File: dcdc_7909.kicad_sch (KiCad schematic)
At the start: 48 parts, among them J1 V_IN, J2 G_IN, J3 Conn_01x01, J4 Conn_01x01, J5 Conn_01x01, J6 Conn_01x01, J7 +10V, J8 G_OUT, J9 -10V, U1 LM2940-SOT223-15, U2 MAX764, U3 LT3045xMSE, U4 LT3094xMSE

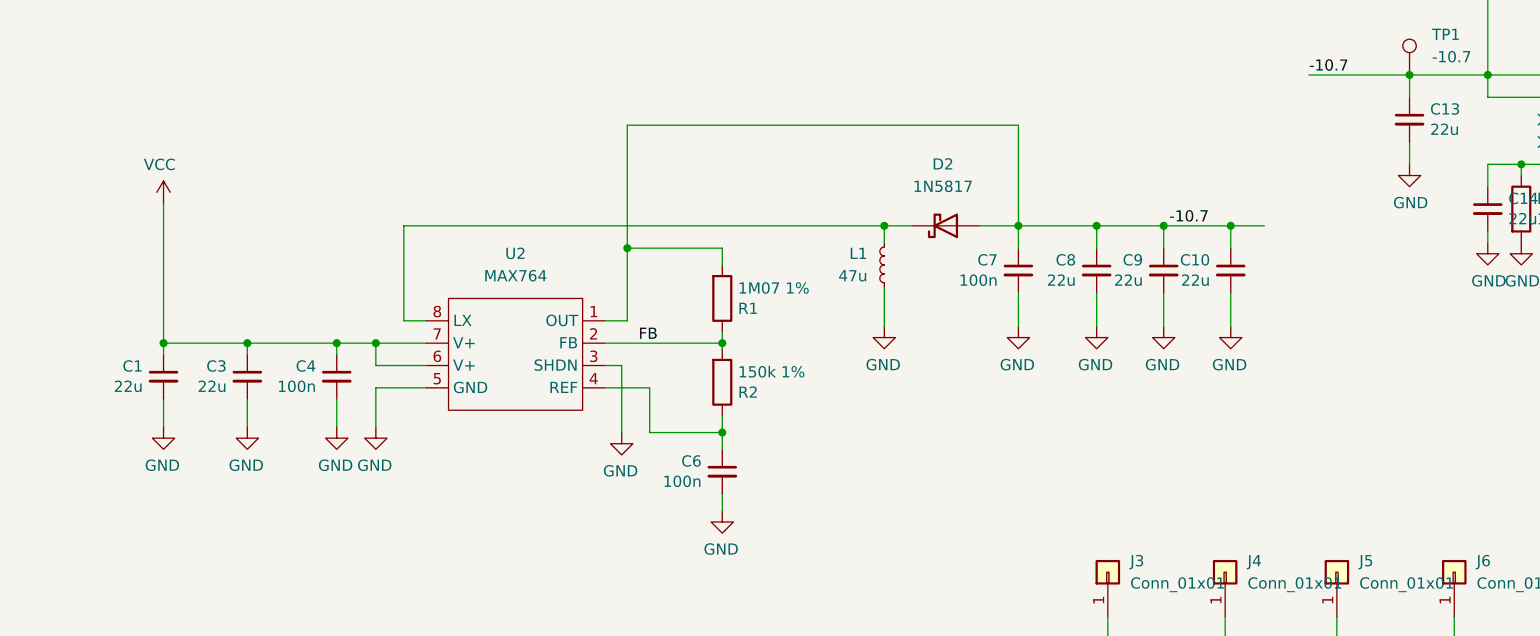
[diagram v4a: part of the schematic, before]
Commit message: Ready design, but MAX764 cannot be used because of the Vin-Vout differential.
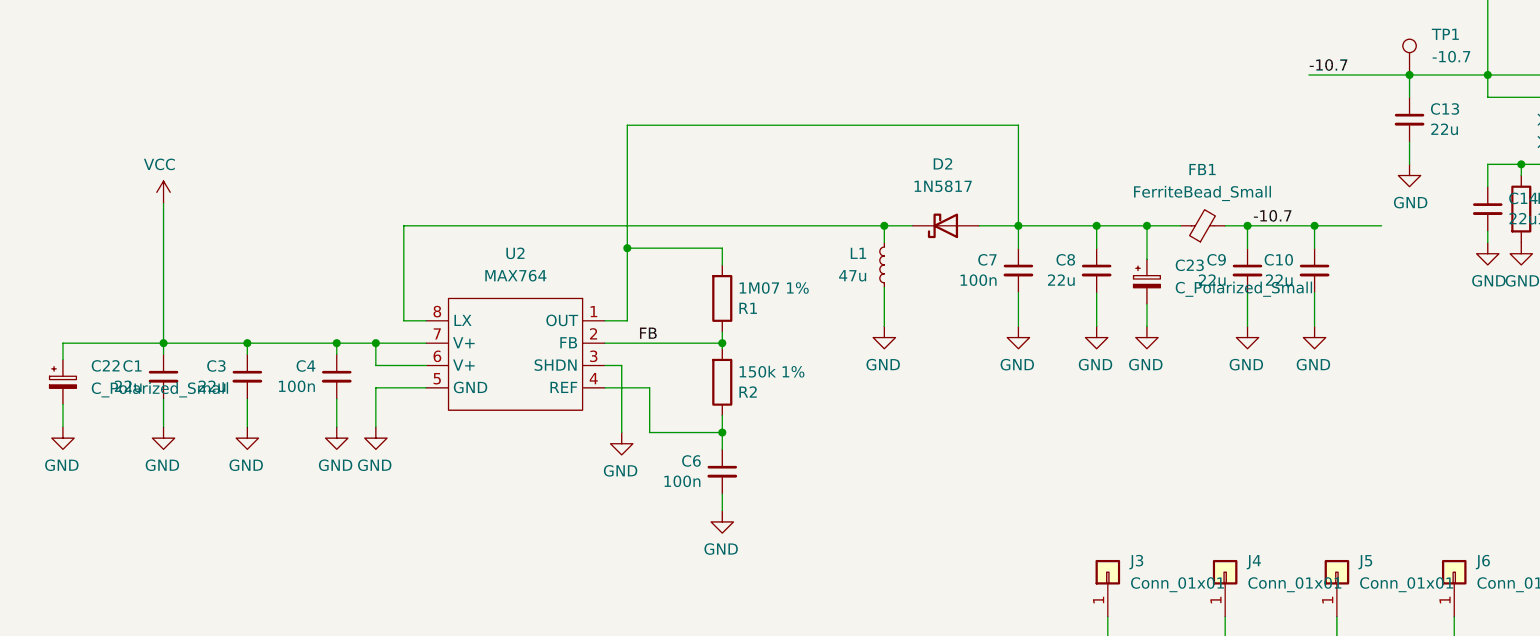
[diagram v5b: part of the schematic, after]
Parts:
- added C22, C23: C_Polarized_Small, Capacitor_Tantalum_SMD:CP_EIA-7343-31_Kemet-D_Pad2.25x2.55mm_HandSolder, symbol Device:C_Polarized_Small
- added FB1: FerriteBead_Small, Resistor_SMD:R_0805_2012Metric, symbol Device:FerriteBead_Small
- D2: LCSC (none) -> C155287
- J3, J4, J5, J6: LCSC (none) -> DO NOT POPULATE
- L1: footprint Inductor_SMD:L_Taiyo-Yuden_NR-60xx -> marcin_library:IND_XGL6060-103MEC
- R1: LCSC C25803 -> C477187
- R2: LCSC C25803 -> C319870
- U2: LCSC (none) -> C143592
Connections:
- net -10.7: now also FB1.2; no longer C7.1, C8.1, D2.2 (A), R1.2, U2.1 (OUT)
- net GND: now also C22.2, C23.2
- net VCC: now also C22.1
- new net: C23.1, C7.1, C8.1, D2.2 (A), FB1.1, R1.2, U2.1 (OUT)
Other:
- moved on the sheet: C10, C9

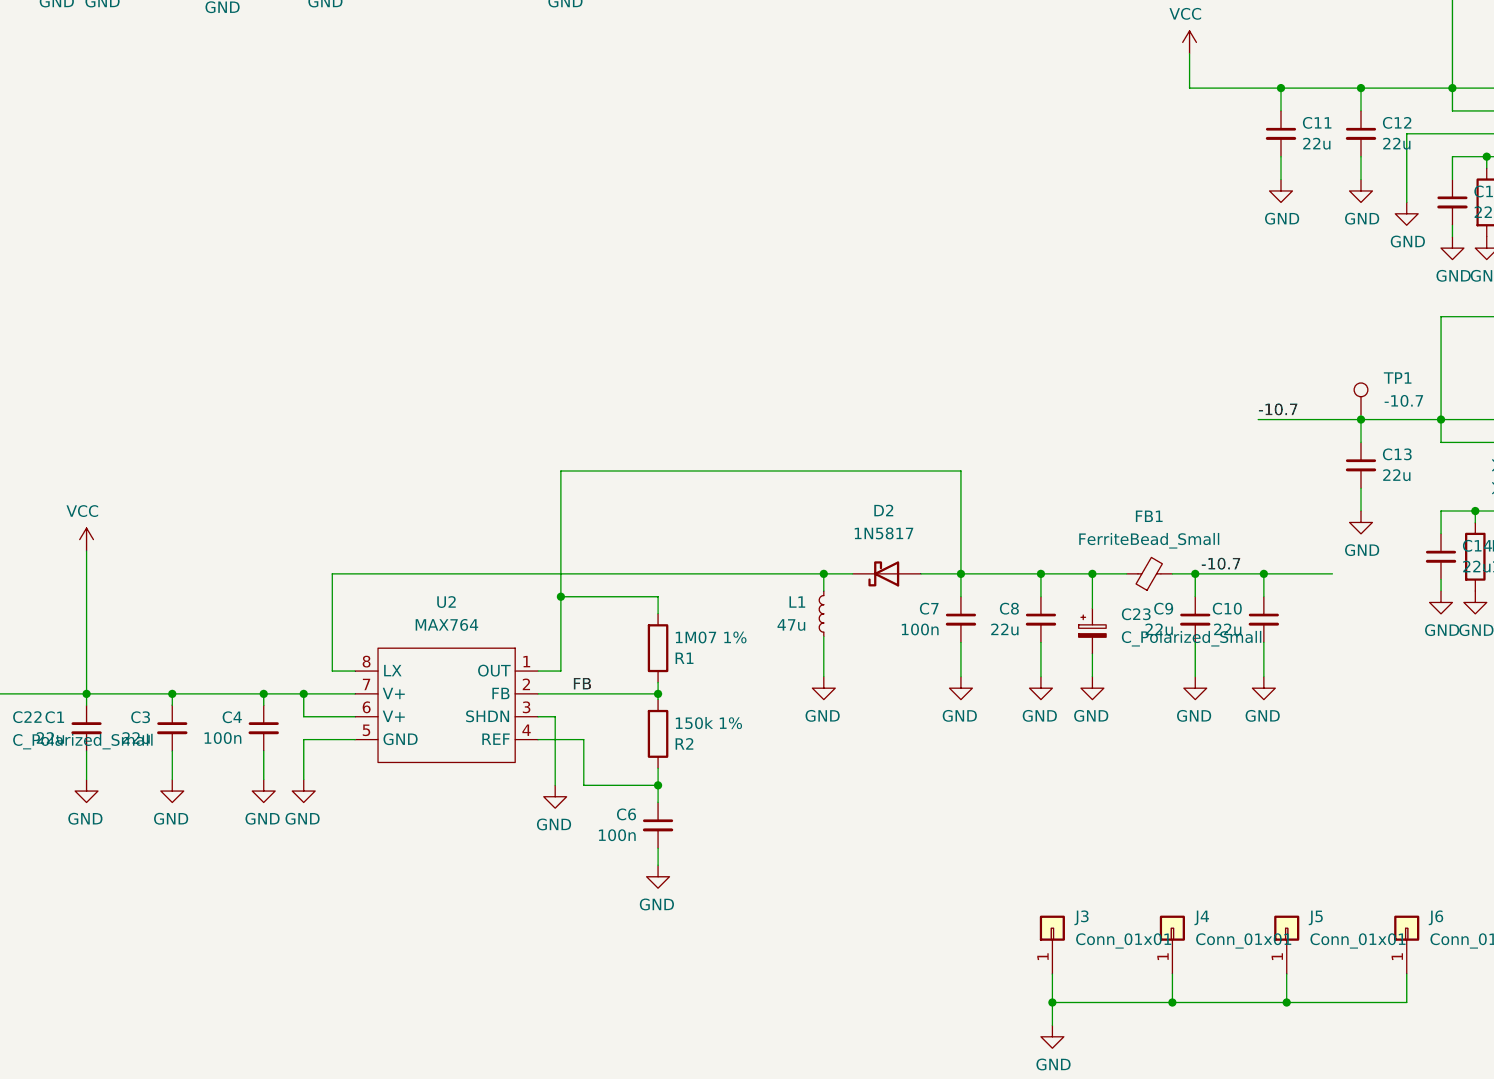
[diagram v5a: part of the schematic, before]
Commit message: Switched to MAX77x + Si9435.
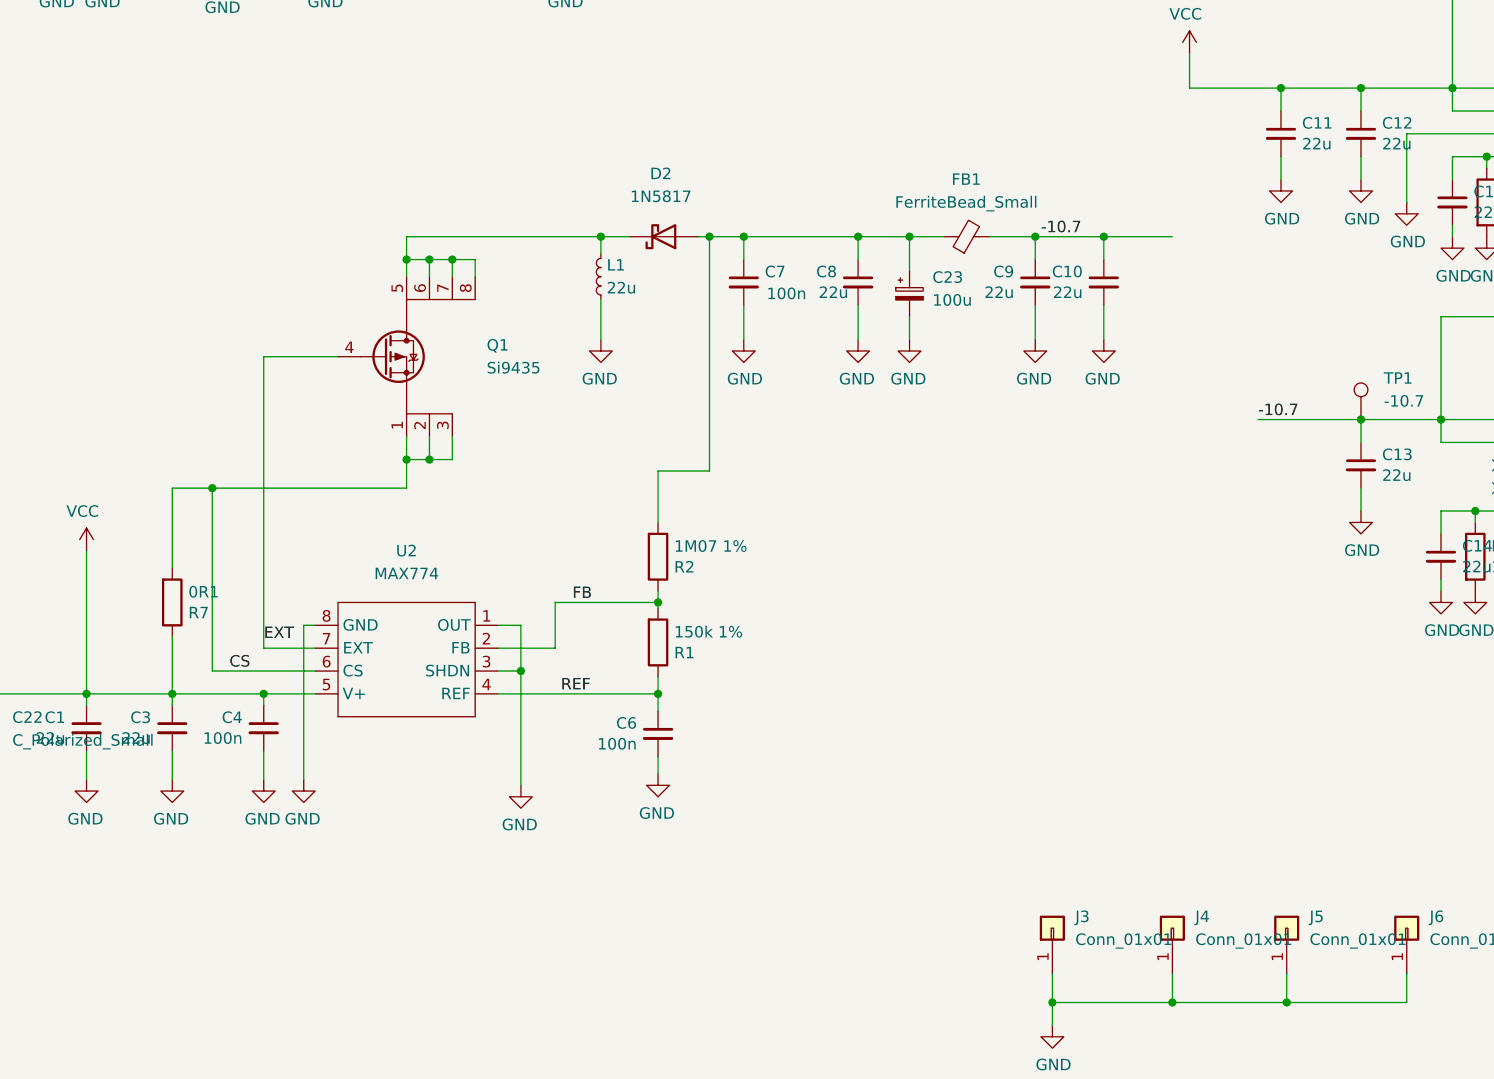
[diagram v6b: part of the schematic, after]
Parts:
- removed U2: MAX764, Package_SO:SO-8_3.9x4.9mm_P1.27mm, symbol marcin_library:MAX764
- added Q1: Si9435, Package_SO:SO-8_3.9x4.9mm_P1.27mm, symbol marcin_library:Si9435
- added R7: 0R1, Resistor_SMD:R_0805_2012Metric, symbol Device:R
- added U2: MAX774, Package_SO:SO-8_3.9x4.9mm_P1.27mm, symbol marcin_library:MAX774
- C23: value C_Polarized_Small -> 100u
- L1: value 47u -> 22u; footprint marcin_library:IND_XGL6060-103MEC -> Inductor_SMD:L_Coilcraft_XxL4040; LCSC (none) -> DO NOT POPULATE
- renumbered R2 to R1, R1 to R2
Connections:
- net FB: now also U2.2 (FB)
- net GND: now also U2.1 (OUT), U2.3 (SHDN), U2.8 (GND)
- net VCC: now also R7.1, U2.5 (V+)
- net at D2.1 (K), L1.1: now also Q1.5 (D), Q1.6 (D), Q1.7 (D), Q1.8 (D)
- net REF: now reaches C6.1, R1.1
- net REF: now also U2.4 (REF)
- new net CS: Q1.1 (S), Q1.2 (S), Q1.3 (S), R7.2, U2.6 (CS)
- new net EXT: Q1.4 (G), U2.7 (EXT)
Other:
- moved on the sheet: C10, C23, C6, C7, C8, C9, D2, FB1, L1, R1, R2

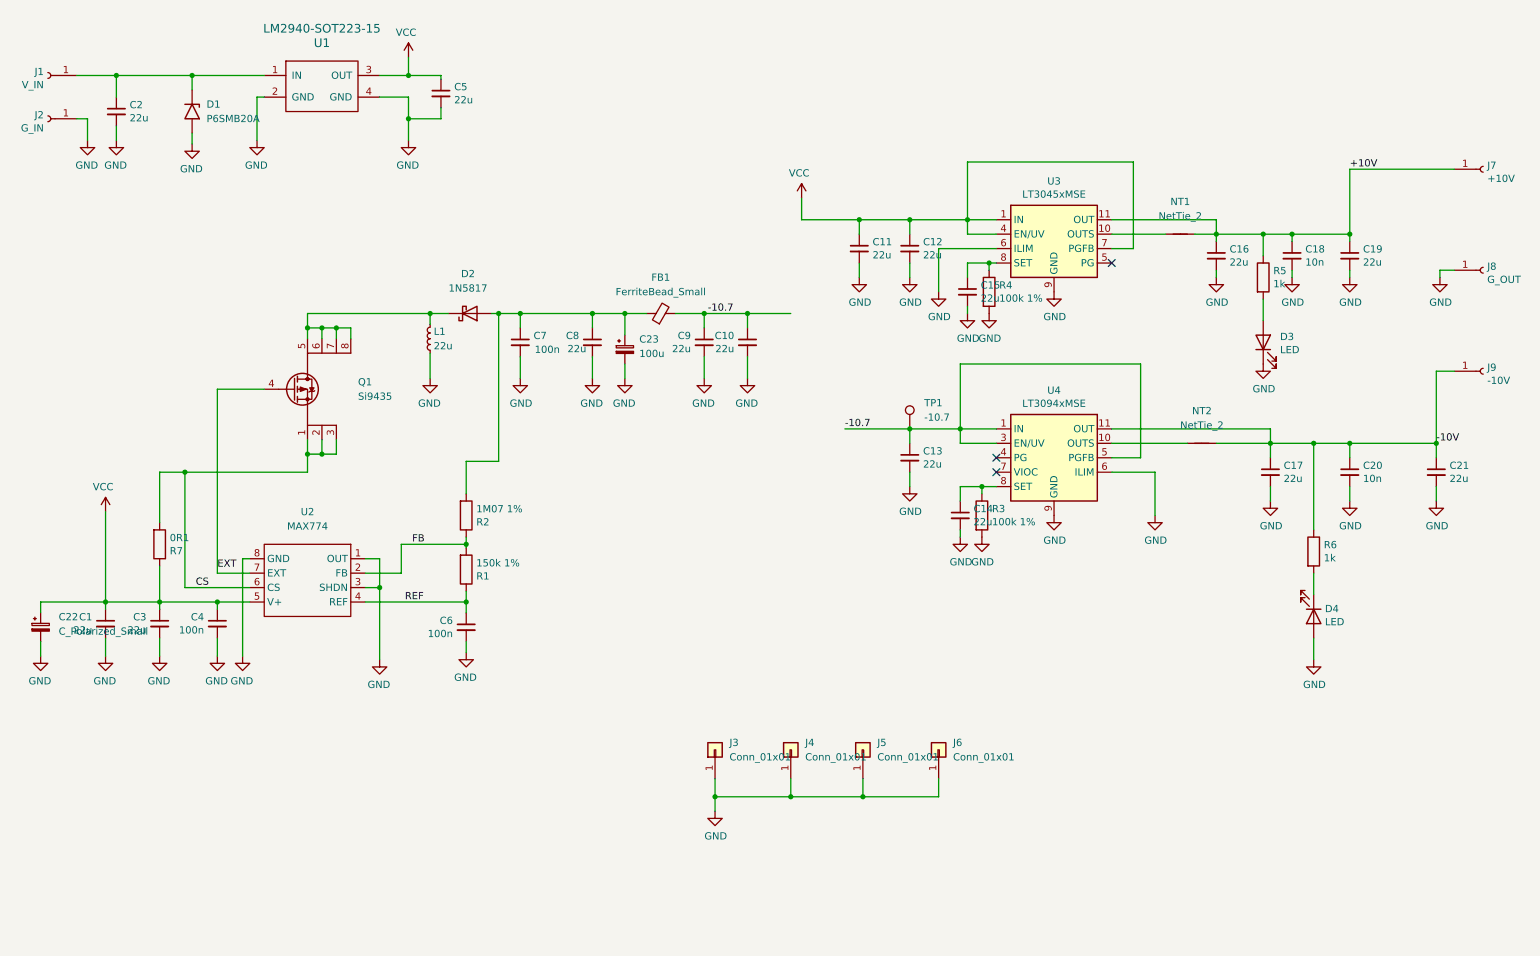
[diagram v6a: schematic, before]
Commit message: Added MAXM15068.
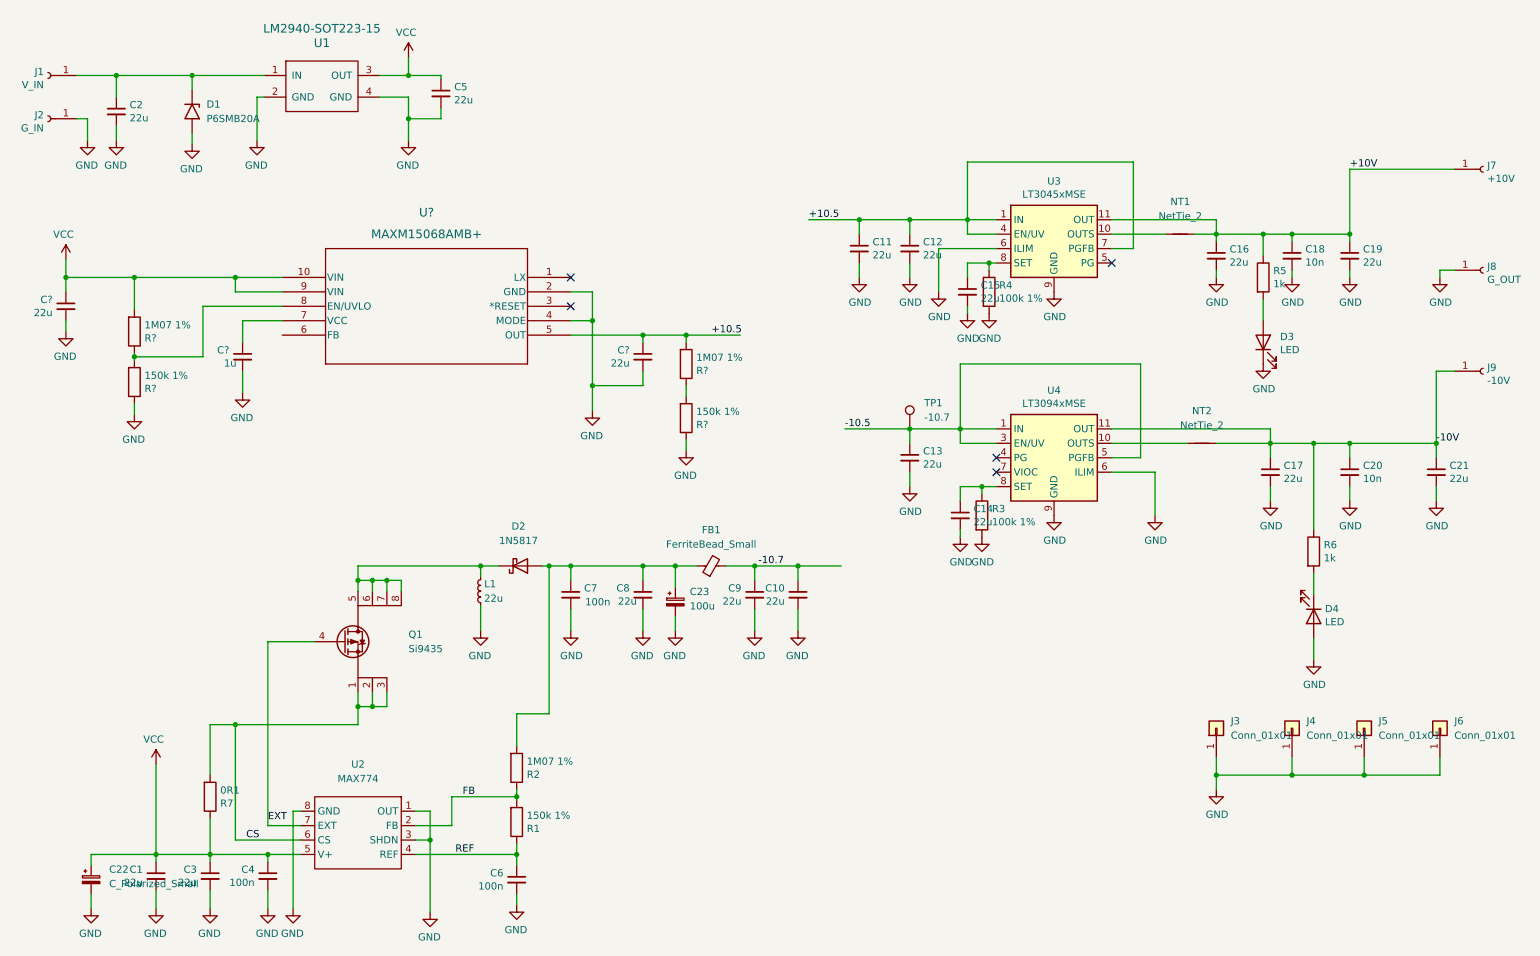
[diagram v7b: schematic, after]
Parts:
- added C?: 1u, Capacitor_SMD:C_1210_3225Metric, symbol Device:C_Small
- added C? (x2): 22u, Capacitor_SMD:C_1210_3225Metric, symbol Device:C_Small
- added R? (x2): 150k 1%, Resistor_SMD:R_0402_1005Metric, symbol Device:R
- added R? (x2): 1M07 1%, Resistor_SMD:R_0402_1005Metric, symbol Device:R
- added U?: MAXM15068AMB+, 21-100094F_M102A3_1, symbol marcin_library:MAXM15068AMB+
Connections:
- net -10.7: no longer C13.1, TP1.1, U4.1 (IN), U4.13 (IN), U4.2 (IN), U4.3 (EN/UV), U4.5 (PGFB)
- net GND: now also C?.2, C?.2, C?.2, R?.1, R?.1, U?.2 (GND), U?.4 (MODE)
- net VCC: now also C?.1, R?.2, U?.10 (VIN), U?.9 (VIN); no longer C11.1, C12.1, U3.1 (IN), U3.2 (IN), U3.3 (IN), U3.4 (EN/UV), U3.7 (PGFB)
- new net: R?.1, R?.2, U?.8 (EN/UVLO)
- new net: C?.1, U?.7 (VCC)
- new net: R?.1, R?.2
- new net +10.5: C11.1, C12.1, C?.1, R?.2, U3.1 (IN), U3.2 (IN), U3.3 (IN), U3.4 (EN/UV), U3.7 (PGFB), U?.5 (OUT)
- new net -10.5: C13.1, TP1.1, U4.1 (IN), U4.13 (IN), U4.2 (IN), U4.3 (EN/UV), U4.5 (PGFB)
- no-connect marks 3 -> 5
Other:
- moved on the sheet: C1, C10, C22, C23, C3, C4, C6, C7, C8, C9, D2, FB1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
